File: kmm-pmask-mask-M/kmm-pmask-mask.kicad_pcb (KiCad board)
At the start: 2 copper layers, 100.4 x 125.7 mm, 78 parts, among them J1 F31L-1A7H1-11030, U1 MS5611-01BA, U10 MAX30101EFD_T, U11 SHT40-AD1B-R3, U12 SHT40-AD1B-R3, U13 TMP117MAIDRVR, U14 TMP117MAIDRVR, U15 TCA9546APW, U2 MAX30101EFD_T, U3 SHT40-AD1B-R3, U4 TMP117MAIDRVR, U5 MS5611-01BA, U6 MS5611-01BA, U7 MS5611-01BA, U8 MAX30101EFD_T, U9 MAX30101EFD_T

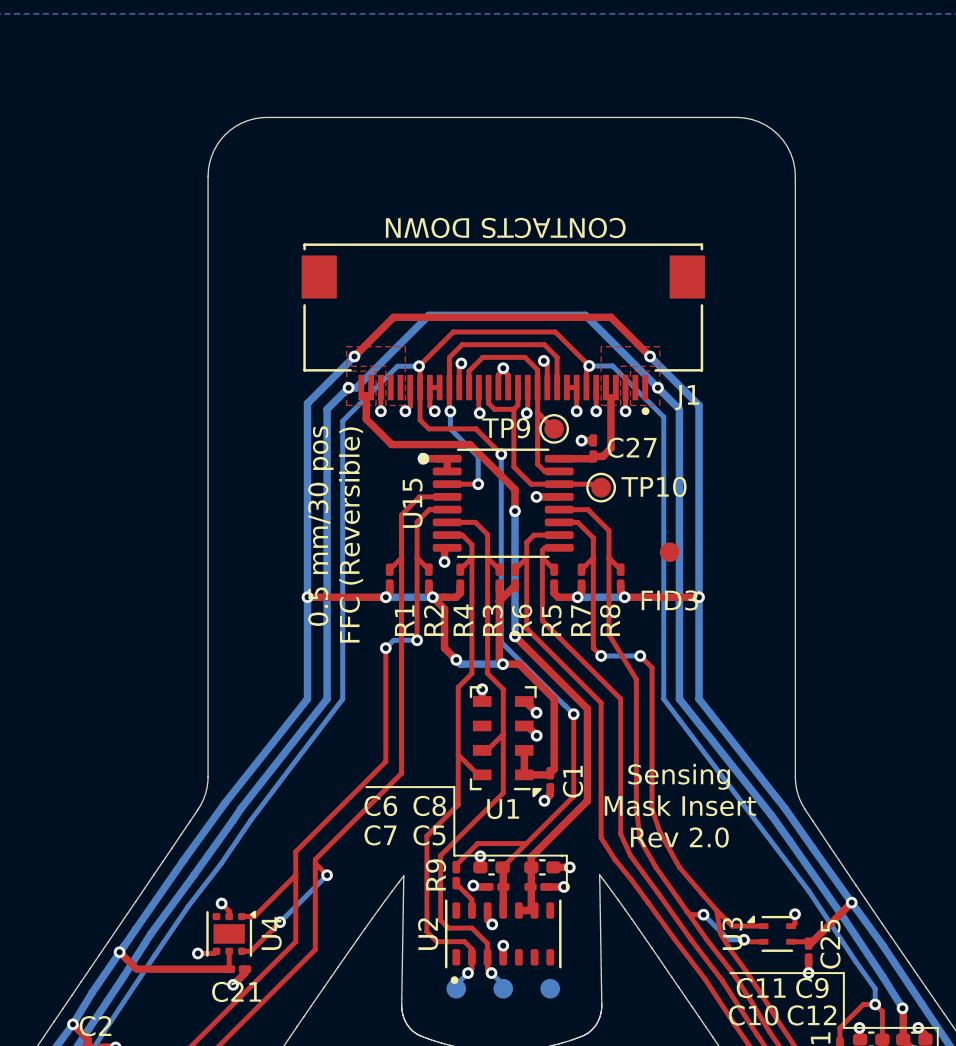
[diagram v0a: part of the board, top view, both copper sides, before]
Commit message: M size profile updated based on ordered XS size board
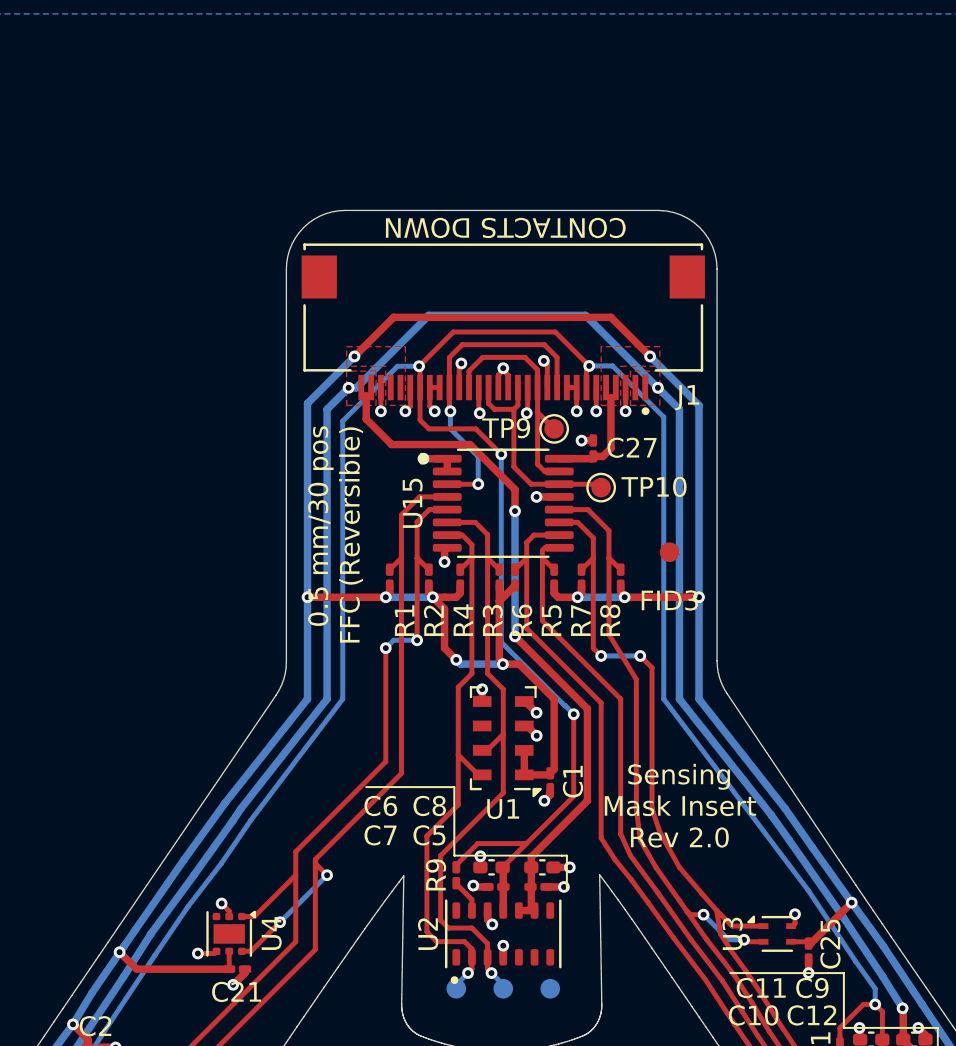
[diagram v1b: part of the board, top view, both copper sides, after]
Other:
- board size 100.4 x 125.7 mm -> 100.4 x 121 mm

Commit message: M size silkscreen updated
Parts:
- removed the G*** at (75.0, 70.0)
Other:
- board text added: "Aiden Lee Xinye Wang Aug 2026"
- board text added: "Sensing Mask Insert Size-M Rev 2.0"
- board text removed: "Sensing Mask Insert Ka Moamoa Lab Rev 2.0"
